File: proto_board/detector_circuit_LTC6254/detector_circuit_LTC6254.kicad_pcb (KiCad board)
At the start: 4 copper layers, 69.2 x 53.2 mm, 43 parts, among them J1 DET_CONN_PWR, J2 SIPM_CONN, J3 DET_CONN, U1 LTC6254

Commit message: moved interfering test point and useless drill holes
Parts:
- removed the REF** at (90.2, 100.5)

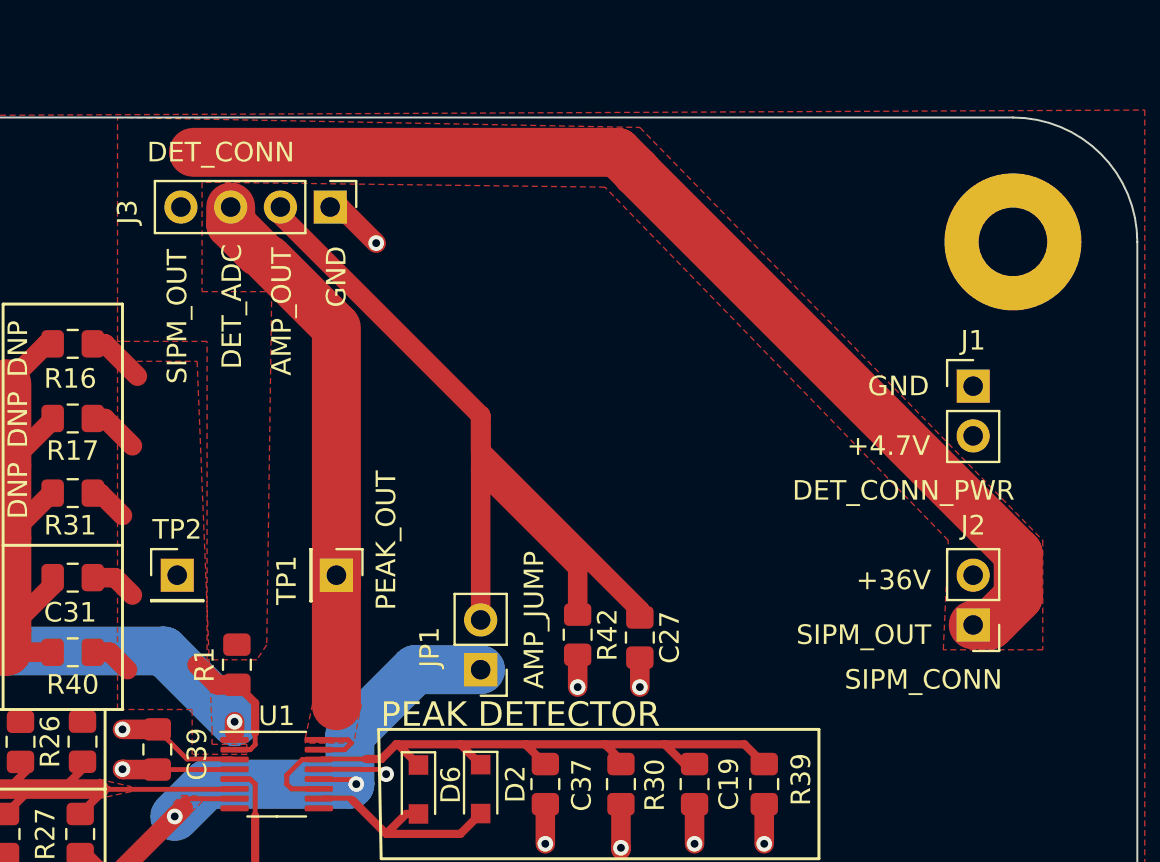
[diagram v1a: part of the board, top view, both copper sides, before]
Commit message: Addressed Zachary's review, re-made gerbers
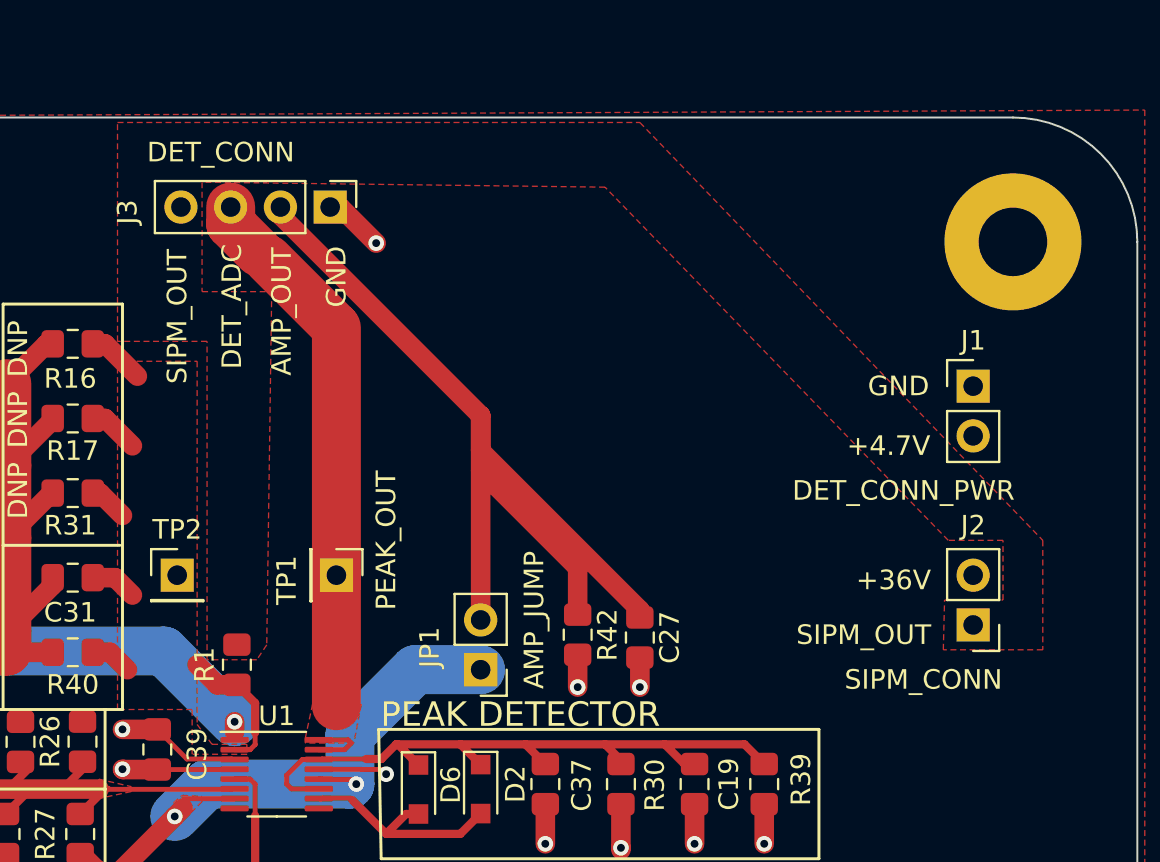
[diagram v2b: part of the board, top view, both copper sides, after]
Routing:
- net /SIPM_OUT: track 55.7 -> 0.00 mm

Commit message: Added dates, fixed some small silkscreen issues generated final gerbers GOOD TO FUCKING GO
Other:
- board text added: "2021-07-15"
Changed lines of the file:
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@@
   (general
     (thickness 1.6)
-    (drawings 60)
+    (drawings 61)
     (tracks 234)
     (zones 0)
@@
   (layers
     (0 Papa.Cu signal)
-    (1 GND.Cu power hide)
-    (2 VCC.Cu power hide)
+    (1 GND.Cu power)
+    (2 VCC.Cu power)
     (31 Mama.Cu signal)
     (32 B.Adhes user hide)
@@
     )
   )
+  (gr_text 2021-07-15 (at 137.287 137.541) (layer F.SilkS)
+    (effects (font (size 1 1) (thickness 0.15)))
+  )
   (dimension 6.35 (width 0.15) (layer Cmts.User)
